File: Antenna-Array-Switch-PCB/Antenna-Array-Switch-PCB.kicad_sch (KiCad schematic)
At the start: 25 parts, among them J101 Conn_SMA, J102 Conn_SMA, J103 Conn_SMA, J104 Conn_Coaxial, U101 LM1117IMP-3.3, U102 SKY13418-485LF

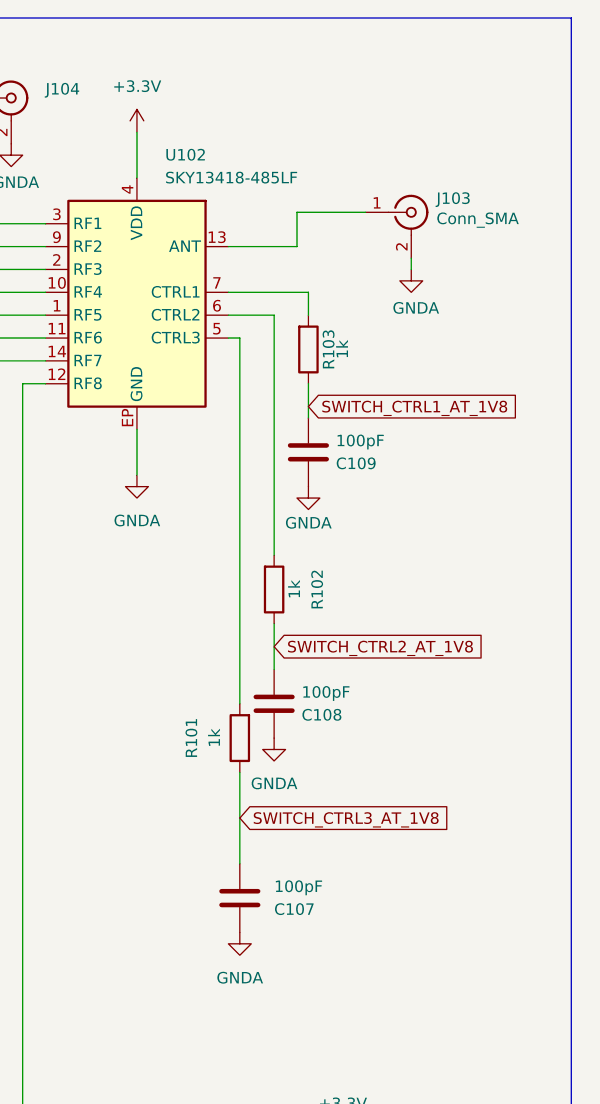
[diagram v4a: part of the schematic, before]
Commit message: PCB: Minor review updates - vias, DC block on switch output
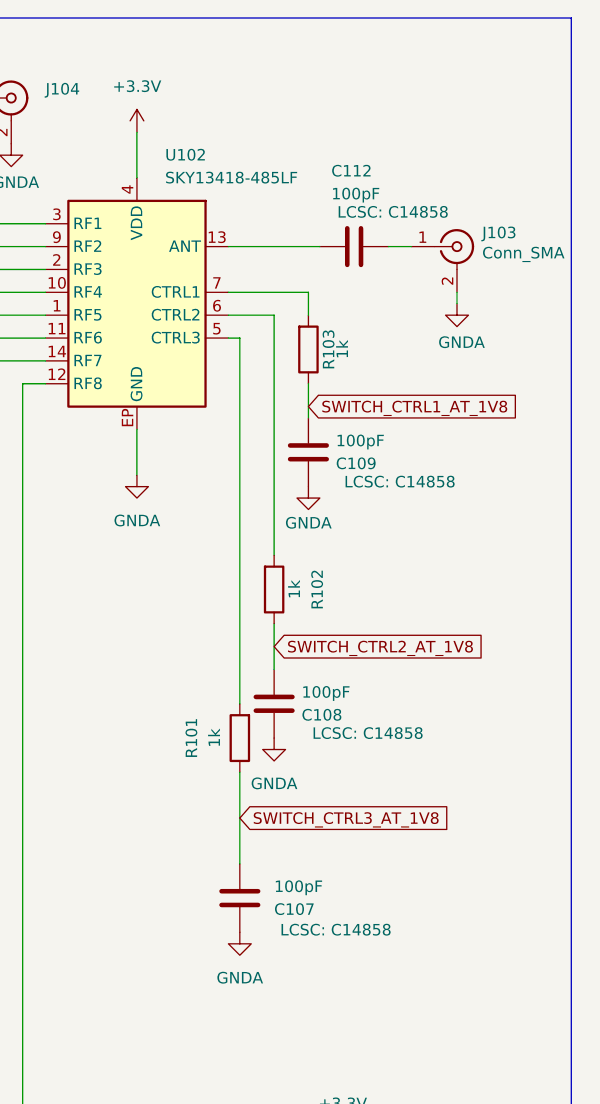
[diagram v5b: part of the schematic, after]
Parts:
- added C112: 100pF, Capacitor_SMD:C_0603_1608Metric_Pad1.08x0.95mm_HandSolder, symbol Device:C
- C107, C108, C109: LCSC (none) -> C14858
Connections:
- net at J103.1 (In): now also C112.1; no longer U102.13 (ANT)
- new net: C112.2, U102.13 (ANT)
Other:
- moved on the sheet: J103
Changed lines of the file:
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@@
 	(wire
 		(pts
-			(xy 234.95 41.91) (xy 242.57 41.91)
-		)
-		(stroke
-			(width 0)
-			(type default)
-		)
-	)
-	(wire
-		(pts
 			(xy 242.57 147.32) (xy 240.03 147.32)
 		)
@@
 	(wire
 		(pts
-			(xy 234.95 41.91) (xy 234.95 45.72)
-		)
-		(stroke
-			(width 0)
-			(type default)
-		)
-	)
-	(wire
-		(pts
 			(xy 57.15 109.22) (xy 57.15 111.76)
 		)
@@
 	(wire
 		(pts
+			(xy 245.11 45.72) (xy 247.65 45.72)
+		)
+		(stroke
+			(width 0)
+			(type default)
+		)
+	)
+	(wire
+		(pts
 			(xy 185.42 45.72) (xy 207.01 45.72)
 		)
@@
 	(wire
 		(pts
-			(xy 234.95 45.72) (xy 227.33 45.72)
+			(xy 227.33 45.72) (xy 237.49 45.72)
 		)
 		(stroke
@@
 	(wire
 		(pts
-			(xy 247.65 48.26) (xy 247.65 46.99)
+			(xy 252.73 52.07) (xy 252.73 50.8)
 		)
 		(stroke
@@
 			)
 		)
+		(property "LCSC" "C14858"
+			(at 246.38 71.882 0)
+			(show_name yes)
+			(do_not_autoplace no)
+			(effects
+				(font
+					(size 1.27 1.27)
+				)
+			)
+		)
 		(pin "1"
 		)
@@
 			)
 		)
+		(property "LCSC" "C14858"
+			(at 242.824 99.822 0)
+			(show_name yes)
+			(do_not_autoplace no)
+			(effects
+				(font
+					(size 1.27 1.27)
+				)
+			)
+		)
 		(pin "1"
 		)
@@
 	)
 	(symbol
+		(lib_id "Device:C")
+		(at 241.3 45.72 270)
+		(mirror x)
+		(unit 1)
+		(body_style 1)
+		(exclude_from_sim no)
+		(in_bom yes)
+		(on_board yes)
+		(in_pos_files yes)
+		(dnp no)
+		(property "Reference" "C112"
+			(at 238.76 37.3379 90)
+			(show_name no)
+			(do_not_autoplace no)
+			(effects
+				(font
+					(size 1.27 1.27)
+				)
+				(justify left)
+			)
+		)
+		(property "Value" "100pF"
+			(at 238.76 39.8779 90)
+			(show_name no)
+			(do_not_autoplace no)
+			(effects
+				(font
+					(size 1.27 1.27)
+				)
+				(justify left)
+			)
+		)
+		(property "Footprint" "Capacitor_SMD:C_0603_1608Metric_Pad1.08x0.95mm_HandSolder"
+			(at 237.49 44.7548 0)
+			(hide yes)
+			(show_name no)
+			(do_not_autoplace no)
+			(effects
+				(font
+					(size 1.27 1.27)
+				)
+			)
+		)
+		(property "Datasheet" ""
+			(at 241.3 45.72 0)
+			(hide yes)
+			(show_name no)
+			(do_not_autoplace no)
+			(effects
+				(font
+					(size 1.27 1.27)
+				)
+			)
+		)
+		(property "Description" "Unpolarized capacitor"
+			(at 241.3 45.72 0)
+			(hide yes)
+			(show_name no)
+			(do_not_autoplace no)
+			(effects
+				(font
+					(size 1.27 1.27)
+				)
+			)
+		)
+		(property "LCSC" "C14858"
+			(at 245.618 41.91 90)
+			(show_name yes)
+			(do_not_autoplace no)
+			(effects
+				(font
+					(size 1.27 1.27)
+				)
+			)
+		)
+		(pin "1"
+		)
+		(pin "2"
+		)
+		(instances
+			(project "Antenna-Array-Switch-PCB"
+				(path "/53a2d682-f221-4d2b-9002-0fe959bb1f68"
+					(reference "C112")
+					(unit 1)
+				)
+			)
+		)
+	)
+	(symbol
 		(lib_id "power:GNDA")
 		(at 203.2 34.29 0)
@@
 	(symbol
 		(lib_id "power:GNDA")
-		(at 247.65 48.26 0)
+		(at 252.73 52.07 0)
 		(unit 1)
 		(body_style 1)
@@
 		(dnp no)
 		(property "Reference" "#PWR0111"
-			(at 247.65 54.61 0)
+			(at 252.73 58.42 0)
 			(hide yes)
 			(show_name no)
@@
 		)
 		(property "Value" "GNDA"
-			(at 248.158 52.578 0)
+			(at 253.238 56.388 0)
 			(show_name no)
 			(do_not_autoplace no)
@@
 		)
 		(property "Footprint" ""
-			(at 247.65 48.26 0)
+			(at 252.73 52.07 0)
 			(hide yes)
 			(show_name no)
@@
 		)
 		(property "Datasheet" ""
-			(at 247.65 48.26 0)
+			(at 252.73 52.07 0)
 			(hide yes)
 			(show_name no)
@@
 		)
 		(property "Description" "Power symbol creates a global label with name \"GNDA\" , analog ground"
-			(at 247.65 48.26 0)
+			(at 252.73 52.07 0)
 			(hide yes)
 			(show_name no)
@@
 			)
 		)
+		(property "LCSC" "C14858"
+			(at 239.268 121.666 0)
+			(show_name yes)
+			(do_not_autoplace no)
+			(effects
+				(font
+					(size 1.27 1.27)
+				)
+			)
+		)
 		(pin "1"
 		)
@@
 	(symbol
 		(lib_id "Connector:Conn_Coaxial")
-		(at 247.65 41.91 0)
+		(at 252.73 45.72 0)
 		(unit 1)
 		(body_style 1)
@@
 		(dnp no)
 		(property "Reference" "J103"
-			(at 250.444 40.386 0)
+			(at 255.524 44.196 0)
 			(show_name no)
 			(do_not_autoplace no)
@@
 		)
 		(property "Value" "Conn_SMA"
-			(at 250.444 42.6329 0)
+			(at 255.524 46.4429 0)
 			(show_name no)
 			(do_not_autoplace no)
@@
 		)
 		(property "Footprint" "Connector_Coaxial:SMA_Amphenol_901-144_Vertical"
-			(at 247.65 41.91 0)
+			(at 252.73 45.72 0)
 			(hide yes)
 			(show_name no)
@@
 		)
 		(property "Datasheet" ""
-			(at 247.65 41.91 0)
+			(at 252.73 45.72 0)
 			(hide yes)
 			(show_name no)
@@
 		)
 		(property "Description" "coaxial connector (BNC, SMA, SMB, SMC, Cinch/RCA, LEMO, ...)"
-			(at 247.65 41.91 0)
+			(at 252.73 45.72 0)
 			(hide yes)
 			(show_name no)

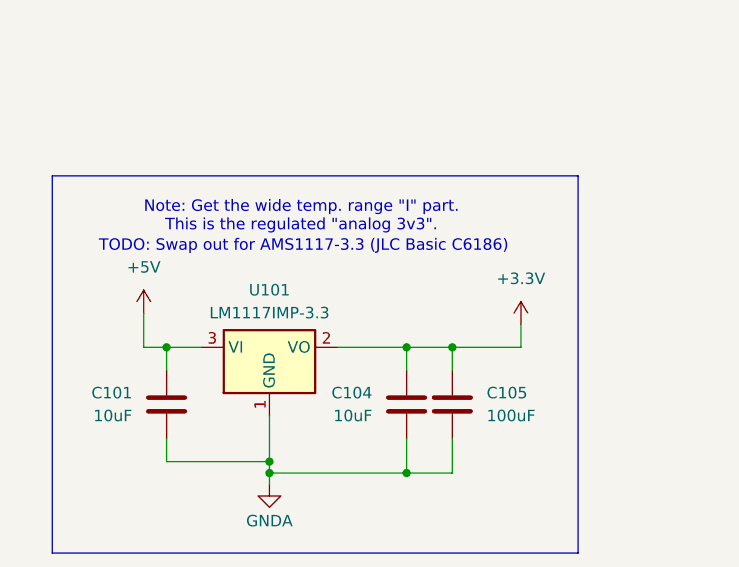
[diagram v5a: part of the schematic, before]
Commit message: PCB: Update regulator to JLC Basic part
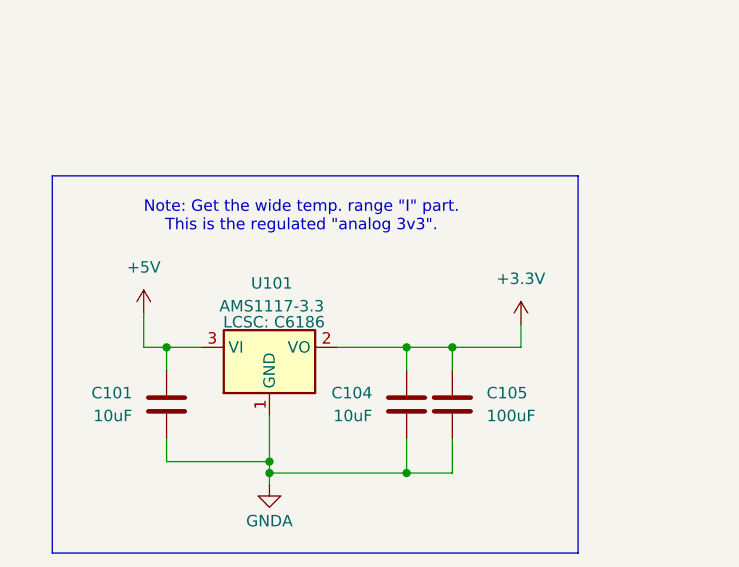
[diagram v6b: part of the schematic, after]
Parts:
- removed U101: LM1117IMP-3.3, Package_TO_SOT_SMD:SOT-223-3_TabPin2, symbol Regulator_Linear:LM1117MP-3.3
- added U101: AMS1117-3.3, Package_TO_SOT_SMD:SOT-223-3_TabPin2, symbol Regulator_Linear:AMS1117-3.3
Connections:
- net +3.3V: now also U101.2 (VO)
- net +5V: now also U101.3 (VI)
- net GNDA: now also U101.1 (GND)
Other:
- note removed: "TODO: Swap out for AMS1117-3.3 (JLC Basic C6186)"
